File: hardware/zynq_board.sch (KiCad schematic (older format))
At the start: 0 parts

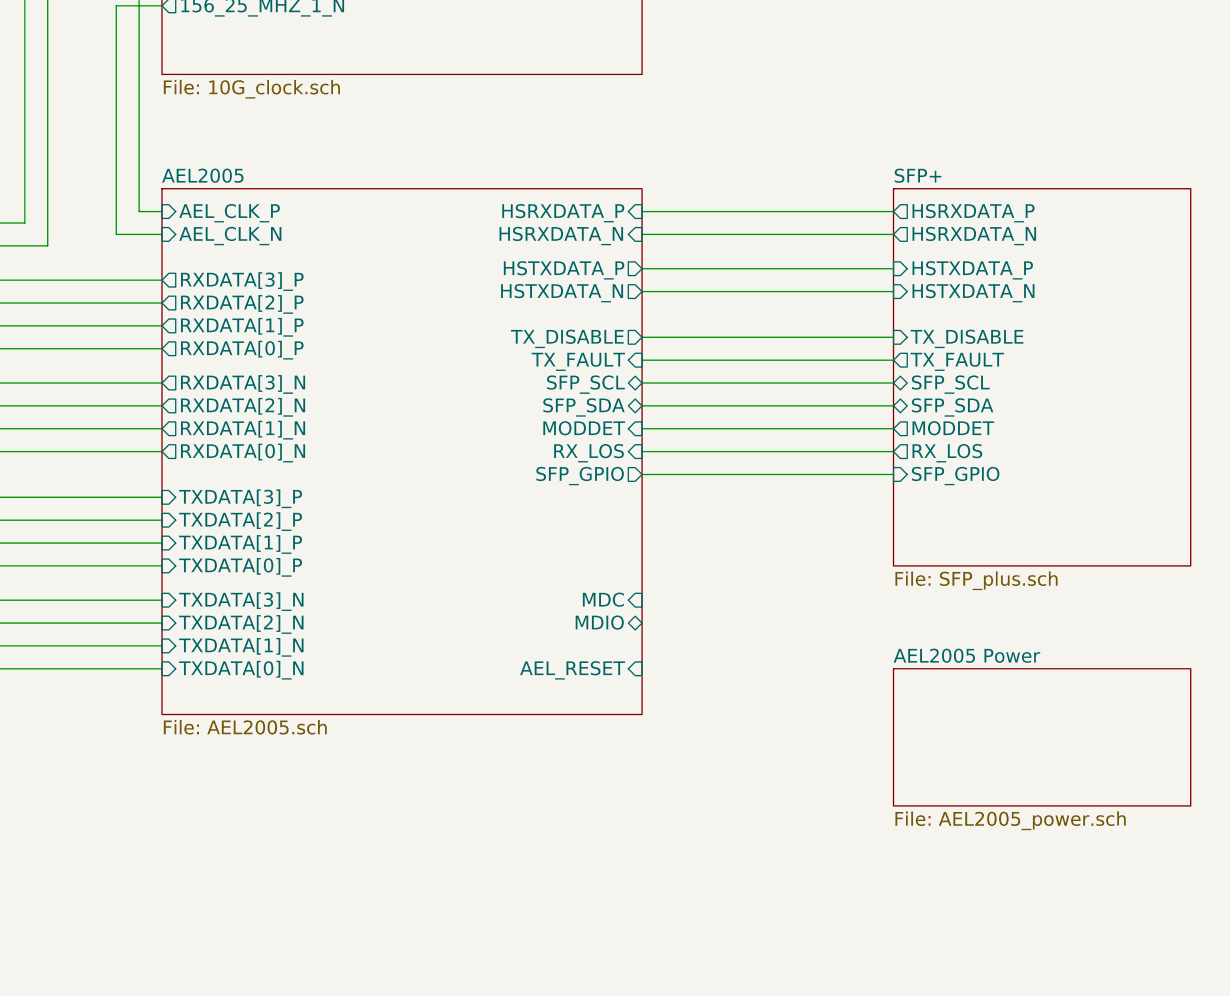
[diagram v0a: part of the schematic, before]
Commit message: Change 10GE interface phy to TLK10031
Low speed signals are still missing. Low speed signals from sfp+ part now need to be connected to the fpga. The new Phy does not support i2c etc..

Also changed KiCad Version to 4.0.7
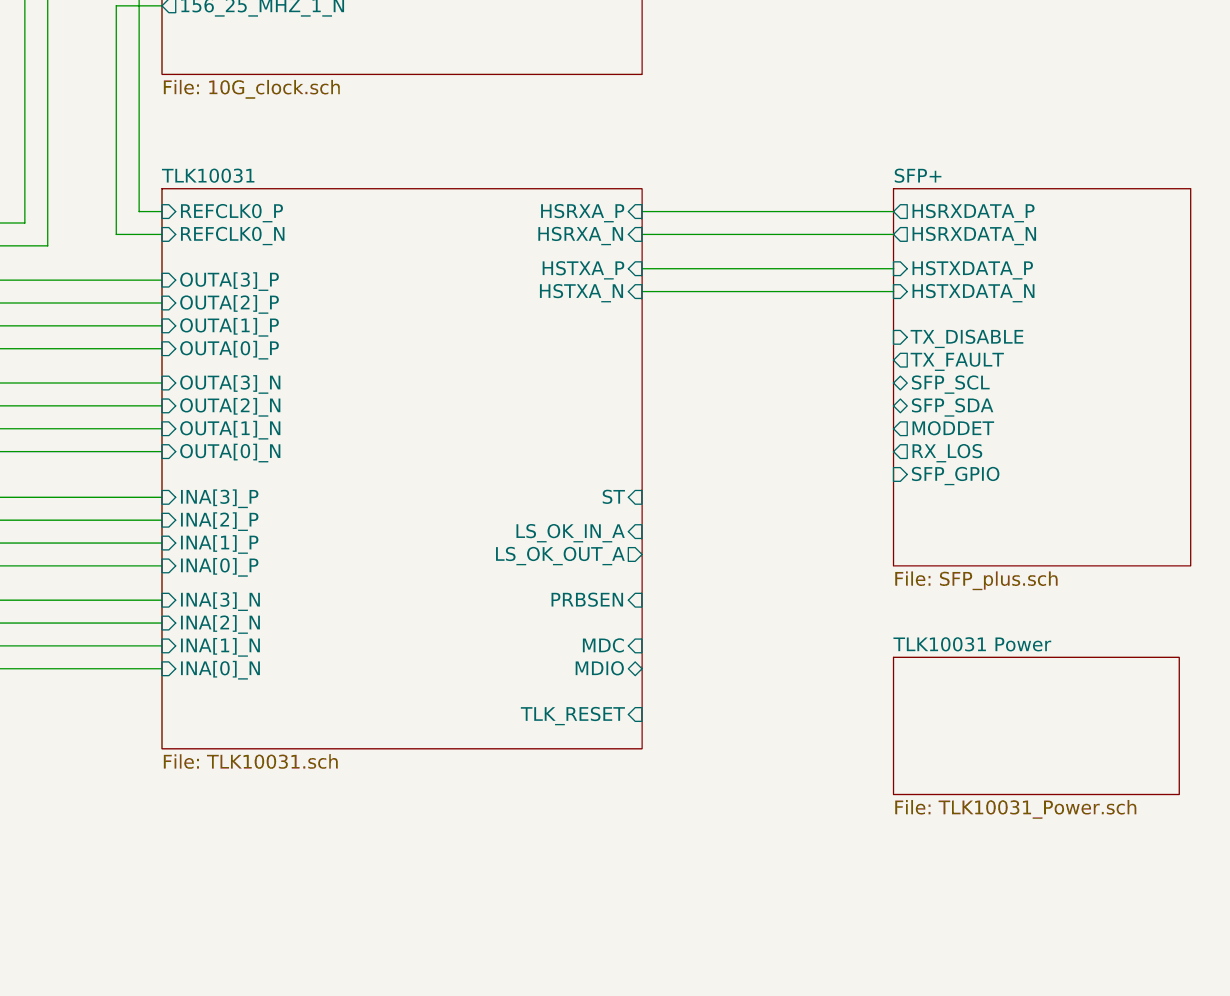
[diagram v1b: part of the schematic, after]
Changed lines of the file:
@@
 EESchema Schematic File Version 2
+LIBS:zynq_board-rescue
 LIBS:power
 LIBS:device
@@
 $EndSheet
 $Sheet
-S 18250 9250 2100 2300
-U 596E816C
-F0 "AEL2005" 60
-F1 "AEL2005.sch" 60
-F2 "AEL_RESET" I R 20350 11350 60
-F3 "HSRXDATA_P" I R 20350 9350 60
-F4 "HSRXDATA_N" I R 20350 9450 60
-F5 "HSTXDATA_P" O R 20350 9600 60
-F6 "HSTXDATA_N" O R 20350 9700 60
-F7 "TX_DISABLE" O R 20350 9900 60
-F8 "RX_LOS" I R 20350 10400 60
-F9 "TX_FAULT" I R 20350 10000 60
-F10 "SFP_GPIO" O R 20350 10500 60
-F11 "MODDET" I R 20350 10300 60
-F12 "SFP_SCL" B R 20350 10100 60
-F13 "SFP_SDA" B R 20350 10200 60
-F14 "AEL_CLK_P" I L 18250 9350 60
-F15 "AEL_CLK_N" I L 18250 9450 60
-F16 "RXDATA[3]_P" O L 18250 9650 60
-F17 "RXDATA[2]_P" O L 18250 9750 60
-F18 "RXDATA[1]_P" O L 18250 9850 60
-F19 "RXDATA[0]_P" O L 18250 9950 60
-F20 "RXDATA[3]_N" O L 18250 10100 60
-F21 "RXDATA[2]_N" O L 18250 10200 60
-F22 "RXDATA[1]_N" O L 18250 10300 60
-F23 "RXDATA[0]_N" O L 18250 10400 60
-F24 "TXDATA[3]_P" I L 18250 10600 60
-F25 "TXDATA[2]_P" I L 18250 10700 60
-F26 "TXDATA[1]_P" I L 18250 10800 60
-F27 "TXDATA[0]_P" I L 18250 10900 60
-F28 "TXDATA[3]_N" I L 18250 11050 60
-F29 "TXDATA[2]_N" I L 18250 11150 60
-F30 "TXDATA[1]_N" I L 18250 11250 60
-F31 "TXDATA[0]_N" I L 18250 11350 60
-F32 "MDIO" B R 20350 11150 60
-F33 "MDC" I R 20350 11050 60
-$EndSheet
-$Sheet
 S 21450 9250 1300 1650
 U 596E8171
@@
 $EndSheet
 $Sheet
-S 21450 11350 1300 600
-U 5974B0D8
-F0 "AEL2005 Power" 60
-F1 "AEL2005_power.sch" 60
-$EndSheet
-$Sheet
 S 18250 7650 2100 1100
 U 597B38C9
@@
 Wire Wire Line
 	13900 11350 18250 11350
-Wire Wire Line
-	20350 9350 21450 9350
-Wire Wire Line
-	21450 9450 20350 9450
-Wire Wire Line
-	20350 9600 21450 9600
-Wire Wire Line
-	21450 9700 20350 9700
-Wire Wire Line
-	20350 9900 21450 9900
-Wire Wire Line
-	21450 10000 20350 10000
-Wire Wire Line
-	20350 10100 21450 10100
-Wire Wire Line
-	21450 10200 20350 10200
-Wire Wire Line
-	20350 10300 21450 10300
-Wire Wire Line
-	21450 10400 20350 10400
 $Sheet
 S 5650 5150 1500 1800
@@
 Text Notes 6100 4150 0    60   ~ 0
 TPS65911 ?
-Wire Wire Line
-	20350 10500 21450 10500
 Wire Bus Line
 	7100 9100 8100 9100
@@
 F1 "zynq_config.sch" 60
 $EndSheet
+$Sheet
+S 18250 9250 2100 2450
+U 5ACA284A
+F0 "TLK10031" 60
+F1 "TLK10031.sch" 60
+F2 "INA[3]_P" I L 18250 10600 60
+F3 "INA[3]_N" I L 18250 11050 60
+F4 "INA[2]_P" I L 18250 10700 60
+F5 "INA[2]_N" I L 18250 11150 60
+F6 "INA[1]_P" I L 18250 10800 60
+F7 "INA[1]_N" I L 18250 11250 60
+F8 "INA[0]_P" I L 18250 10900 60
+F9 "INA[0]_N" I L 18250 11350 60
+F10 "OUTA[3]_P" I L 18250 9650 60
+F11 "OUTA[3]_N" I L 18250 10100 60
+F12 "OUTA[2]_P" I L 18250 9750 60
+F13 "OUTA[2]_N" I L 18250 10200 60
+F14 "OUTA[1]_P" I L 18250 9850 60
+F15 "OUTA[1]_N" I L 18250 10300 60
+F16 "OUTA[0]_P" I L 18250 9950 60
+F17 "OUTA[0]_N" I L 18250 10400 60
+F18 "REFCLK0_P" I L 18250 9350 60
+F19 "REFCLK0_N" I L 18250 9450 60
+F20 "HSTXA_P" I R 20350 9600 60
+F21 "HSTXA_N" I R 20350 9700 60
+F22 "HSRXA_P" I R 20350 9350 60
+F23 "HSRXA_N" I R 20350 9450 60
+F24 "TLK_RESET" I R 20350 11550 60
+F25 "MDC" I R 20350 11250 60
+F26 "LS_OK_IN_A" I R 20350 10750 60
+F27 "LS_OK_OUT_A" O R 20350 10850 60
+F28 "ST" I R 20350 10600 60
+F29 "PRBSEN" I R 20350 11050 60
+F30 "MDIO" B R 20350 11350 60
+$EndSheet
+$Sheet
+S 21450 11300 1250 600
+U 5ACA2ECE
+F0 "TLK10031 Power" 60
+F1 "TLK10031_Power.sch" 60
+$EndSheet
+Wire Wire Line
+	20350 9350 21450 9350
+Wire Wire Line
+	21450 9450 20350 9450
+Wire Wire Line
+	20350 9600 21450 9600
+Wire Wire Line
+	21450 9700 20350 9700
 $EndSCHEMATC

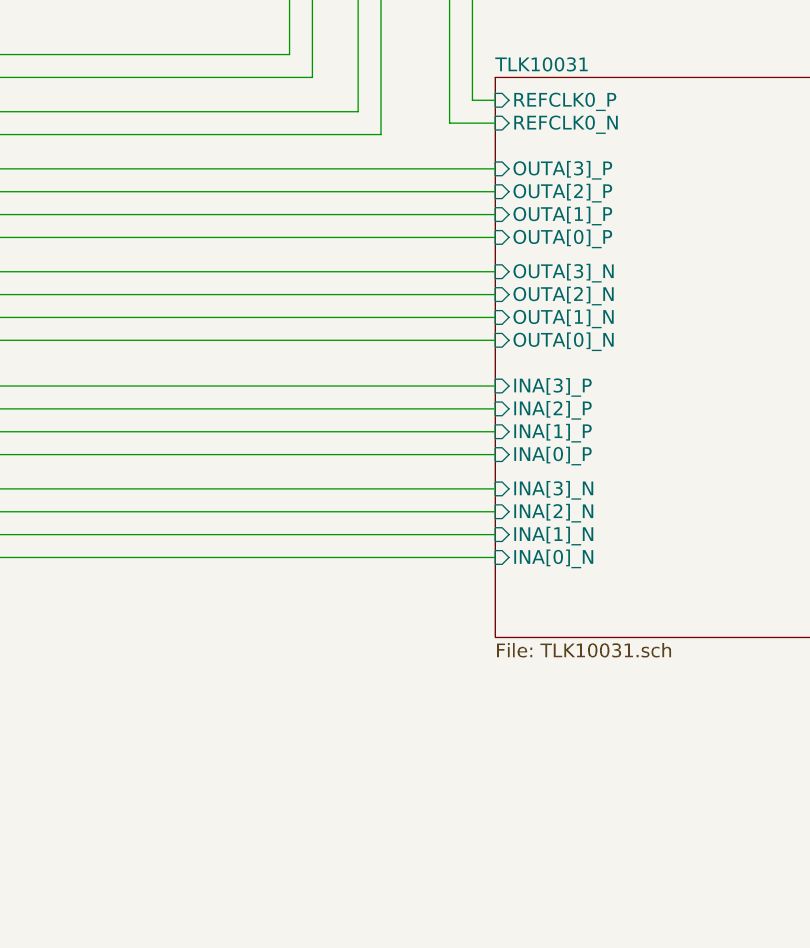
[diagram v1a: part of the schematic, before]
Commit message: Changed TLK VDDO Voltage to 1V8 and corrected hierachical Pin direction
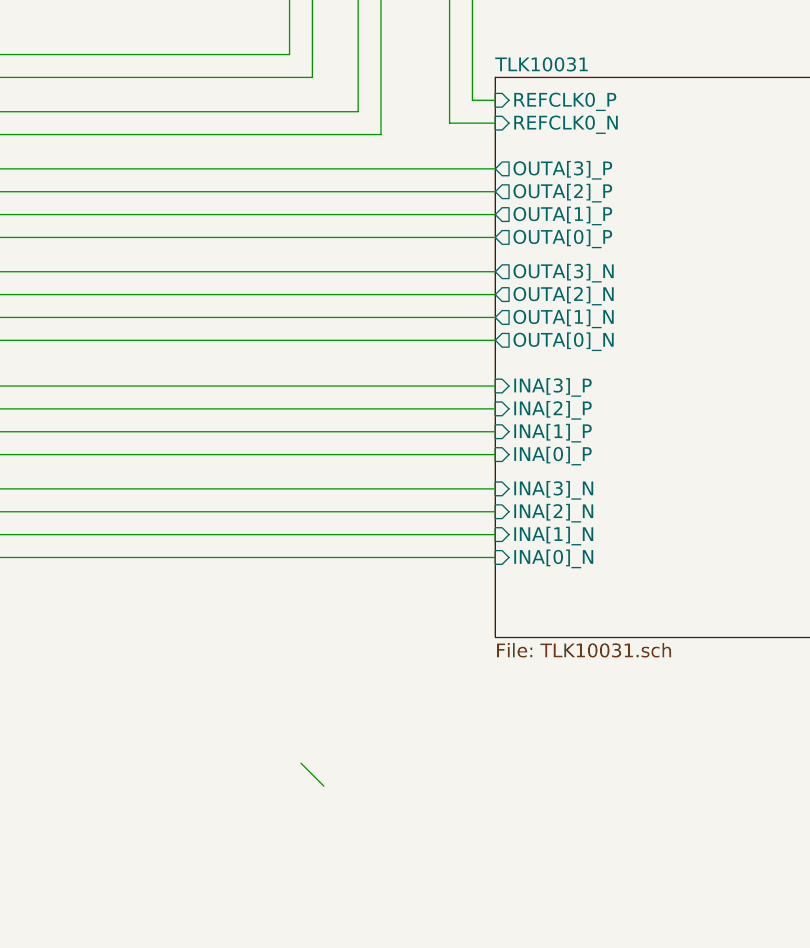
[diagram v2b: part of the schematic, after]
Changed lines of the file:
@@
-$EndSheet
-$Sheet
-S 18250 9250 2100 2450
-U 5ACA284A
-F0 "TLK10031" 60
-F1 "TLK10031.sch" 60
-F2 "INA[3]_P" I L 18250 10600 60
-F3 "INA[3]_N" I L 18250 11050 60
-F4 "INA[2]_P" I L 18250 10700 60
-F5 "INA[2]_N" I L 18250 11150 60
-F6 "INA[1]_P" I L 18250 10800 60
-F7 "INA[1]_N" I L 18250 11250 60
-F8 "INA[0]_P" I L 18250 10900 60
-F9 "INA[0]_N" I L 18250 11350 60
-F10 "OUTA[3]_P" I L 18250 9650 60
-F11 "OUTA[3]_N" I L 18250 10100 60
-F12 "OUTA[2]_P" I L 18250 9750 60
-F13 "OUTA[2]_N" I L 18250 10200 60
-F14 "OUTA[1]_P" I L 18250 9850 60
-F15 "OUTA[1]_N" I L 18250 10300 60
-F16 "OUTA[0]_P" I L 18250 9950 60
-F17 "OUTA[0]_N" I L 18250 10400 60
-F18 "REFCLK0_P" I L 18250 9350 60
-F19 "REFCLK0_N" I L 18250 9450 60
-F20 "HSTXA_P" I R 20350 9600 60
-F21 "HSTXA_N" I R 20350 9700 60
-F22 "HSRXA_P" I R 20350 9350 60
-F23 "HSRXA_N" I R 20350 9450 60
-F24 "TLK_RESET" I R 20350 11550 60
-F25 "MDC" I R 20350 11250 60
-F26 "LS_OK_IN_A" I R 20350 10750 60
-F27 "LS_OK_OUT_A" O R 20350 10850 60
-F28 "ST" I R 20350 10600 60
-F29 "PRBSEN" I R 20350 11050 60
-F30 "MDIO" B R 20350 11350 60
 $EndSheet
 $Sheet
@@
 Wire Wire Line
 	21450 9700 20350 9700
+Entry Wire Line
+	17400 12250 17500 12350
+$Sheet
+S 18250 9250 2100 2450
+U 5ACA284A
+F0 "TLK10031" 60
+F1 "TLK10031.sch" 60
+F2 "INA[3]_P" I L 18250 10600 60
+F3 "INA[3]_N" I L 18250 11050 60
+F4 "INA[2]_P" I L 18250 10700 60
+F5 "INA[2]_N" I L 18250 11150 60
+F6 "INA[1]_P" I L 18250 10800 60
+F7 "INA[1]_N" I L 18250 11250 60
+F8 "INA[0]_P" I L 18250 10900 60
+F9 "INA[0]_N" I L 18250 11350 60
+F10 "REFCLK0_P" I L 18250 9350 60
+F11 "REFCLK0_N" I L 18250 9450 60
+F12 "HSTXA_P" I R 20350 9600 60
+F13 "HSTXA_N" I R 20350 9700 60
+F14 "HSRXA_P" I R 20350 9350 60
+F15 "HSRXA_N" I R 20350 9450 60
+F16 "TLK_RESET" I R 20350 11550 60
+F17 "MDC" I R 20350 11250 60
+F18 "LS_OK_IN_A" I R 20350 10750 60
+F19 "LS_OK_OUT_A" O R 20350 10850 60
+F20 "ST" I R 20350 10600 60
+F21 "PRBSEN" I R 20350 11050 60
+F22 "MDIO" B R 20350 11350 60
+F23 "OUTA[3]_P" O L 18250 9650 60
+F24 "OUTA[3]_N" O L 18250 10100 60
+F25 "OUTA[2]_P" O L 18250 9750 60
+F26 "OUTA[2]_N" O L 18250 10200 60
+F27 "OUTA[1]_P" O L 18250 9850 60
+F28 "OUTA[1]_N" O L 18250 10300 60
+F29 "OUTA[0]_P" O L 18250 9950 60
+F30 "OUTA[0]_N" O L 18250 10400 60
+$EndSheet
 $EndSCHEMATC

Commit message: Drew missing 10 G Phy Lowspeed Signals.
Also moved the SFP+ Lowspeedsignals a bit to ease routing
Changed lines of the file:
@@
 $EndDescr
 $Sheet
-S 4250 3750 2750 1250
+S 4250 2400 2750 2650
 U 596E752F
 F0 "Power" 60
@@
 $EndSheet
 $Sheet
-S 7300 3750 2750 750
+S 7300 2400 2750 2100
 U 596E75FA
 F0 "PL: Bank 34" 60
@@
 F7 "TX_FAULT_18" I R 10050 4300 60
 F8 "TX_DISABLE_18" O R 10050 4400 60
-$EndSheet
-Text Notes 5000 3350 0    197  ~ 39
+F9 "ST" O R 10050 3500 60
+F10 "LS_OK_IN_A" O R 10050 3400 60
+F11 "LS_OK_OUT_A" I R 10050 3300 60
+F12 "PRBSEN" O R 10050 3200 60
+F13 "MDC" O R 10050 3100 60
+F14 "MDIO" B R 10050 3000 60
+F15 "TLK_RESET" O R 10050 2900 60
+$EndSheet
+Text Notes 4900 2050 0    197  ~ 39
 ZYNQ 7012S / 7015 / 7030
 $Sheet
@@
 $EndSheet
 $Sheet
-S 1800 3750 1500 1250
+S 1800 2400 1500 1250
 U 596E8178
 F0 "PMIC" 60
@@
 F15 "RESETB" I R 3300 6800 60
 $EndSheet
-Text Notes 2250 4300 0    60   ~ 0
+Text Notes 2250 3050 0    60   ~ 0
 TPS65911 ?
 $Sheet
@@
 $EndSheet
 Wire Notes Line
-	4050 3500 4050 13200
+	4050 2200 4050 13200
 Wire Notes Line
 	4050 13200 10250 13200
 Wire Notes Line
-	10250 13200 10250 3500
-Wire Notes Line
-	10250 3500 4050 3500
+	10250 13200 10250 2200
 Wire Wire Line
 	10050 9300 16500 9300
@@
 Wire Wire Line
 	10050 6700 11750 6700
+Wire Notes Line
+	10250 2200 4050 2200
+Wire Wire Line
+	19500 11350 21850 11350
+Wire Wire Line
+	21850 11350 21850 2850
+Wire Wire Line
+	21850 2850 14250 2850
+Wire Wire Line
+	14250 2850 14250 3500
+Wire Wire Line
+	14250 3500 10050 3500
+Wire Wire Line
+	19500 11500 21950 11500
+Wire Wire Line
+	21950 11500 21950 2750
+Wire Wire Line
+	21950 2750 14150 2750
+Wire Wire Line
+	14150 2750 14150 3400
+Wire Wire Line
+	14150 3400 10050 3400
+Wire Wire Line
+	10050 3300 14050 3300
+Wire Wire Line
+	14050 3300 14050 2650
+Wire Wire Line
+	14050 2650 22050 2650
+Wire Wire Line
+	22050 2650 22050 11600
+Wire Wire Line
+	22050 11600 19500 11600
+Wire Wire Line
+	19500 11750 22150 11750
+Wire Wire Line
+	22150 11750 22150 2550
+Wire Wire Line
+	22150 2550 13950 2550
+Wire Wire Line
+	13950 2550 13950 3200
+Wire Wire Line
+	13950 3200 10050 3200
+Wire Wire Line
+	10050 3100 13850 3100
+Wire Wire Line
+	13850 3100 13850 2450
+Wire Wire Line
+	13850 2450 22250 2450
+Wire Wire Line
+	22250 2450 22250 11900
+Wire Wire Line
+	22250 11900 19500 11900
+Wire Wire Line
+	19500 12000 22350 12000
+Wire Wire Line
+	22350 12000 22350 2350
+Wire Wire Line
+	22350 2350 13750 2350
+Wire Wire Line
+	13750 2350 13750 3000
+Wire Wire Line
+	13750 3000 10050 3000
+Wire Wire Line
+	10050 2900 13650 2900
+Wire Wire Line
+	13650 2900 13650 2250
+Wire Wire Line
+	13650 2250 22450 2250
+Wire Wire Line
+	22450 2250 22450 12150
+Wire Wire Line
+	22450 12150 19500 12150
 $EndSCHEMATC
